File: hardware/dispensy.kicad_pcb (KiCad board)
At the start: 2 copper layers, 125 x 90 mm, 90 parts, among them SW1 BOOTSEL, SW2 RESET, U1 DBT50G-7_62-4P, U10 RP2040, U11 SS54, U12 SS54_C22452, U13 CAN_IO, U14 TJA1042T_3_1J, U15 USB-C, U16 LM2576S-5_0_TR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

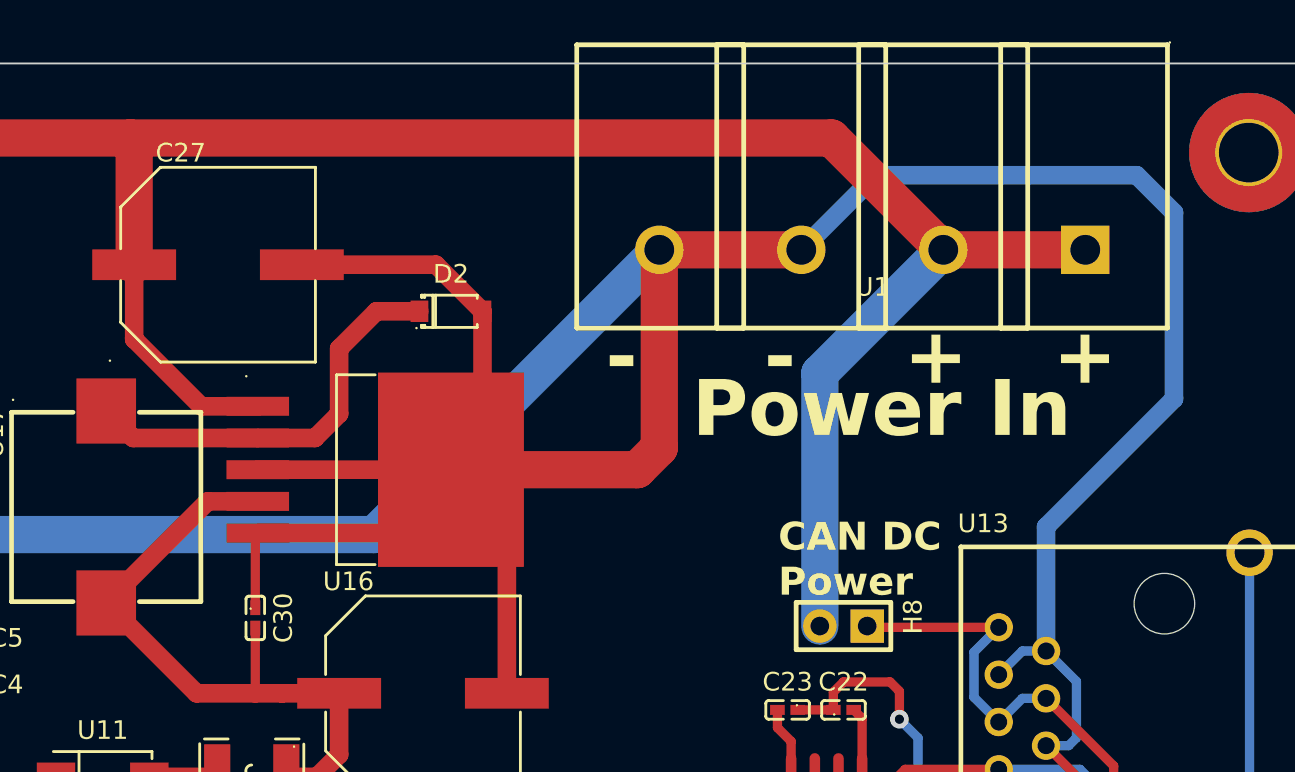
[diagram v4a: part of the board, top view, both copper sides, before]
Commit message: more distance between mounting hole and power connector.
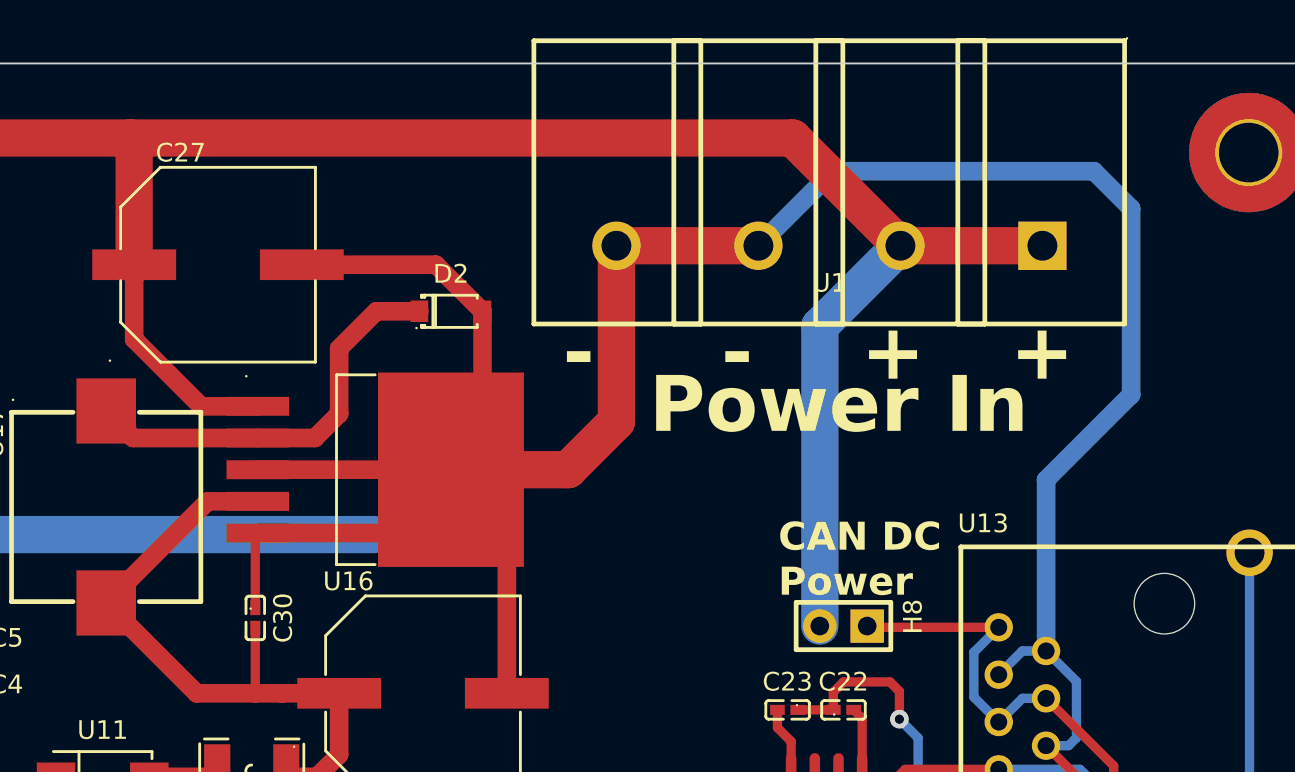
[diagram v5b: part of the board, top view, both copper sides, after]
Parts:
- moved U1 2.31 mm to (191.0, 57.5)
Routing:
- net GND: track 499.6 -> 474.3 mm
- net +VDC: track 126.2 -> 123.0 mm

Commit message: some more routing
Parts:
- moved C1 0.41 mm to (191.9, 109.8)
- moved OLED1 0.41 mm to (181.1, 137.0)
- moved R1 0.41 mm to (194.9, 109.8)
- moved R2 0.41 mm to (197.5, 109.8)
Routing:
- net +5V: track 37.0 -> 81.7 mm, vias 2 -> 8
- net GND: track 474.3 -> 498.2 mm

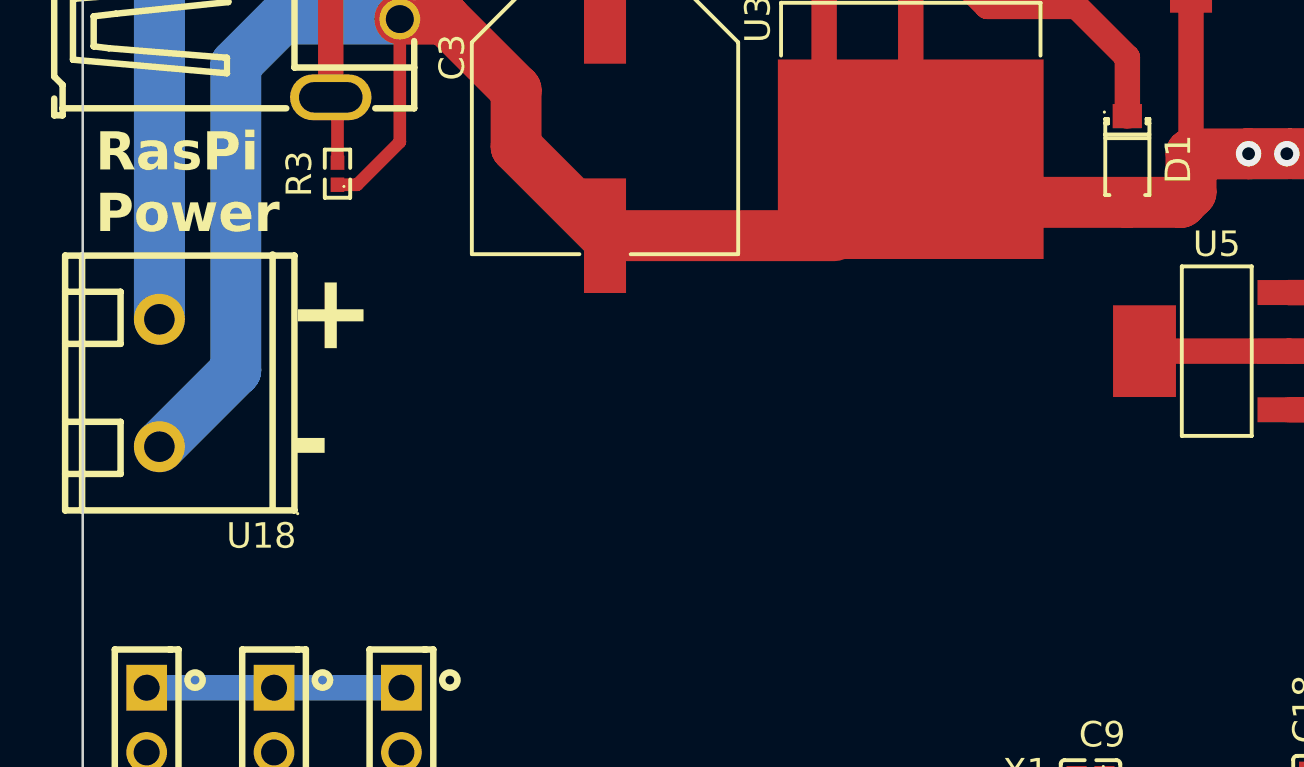
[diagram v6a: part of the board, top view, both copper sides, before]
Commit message: add power status leds
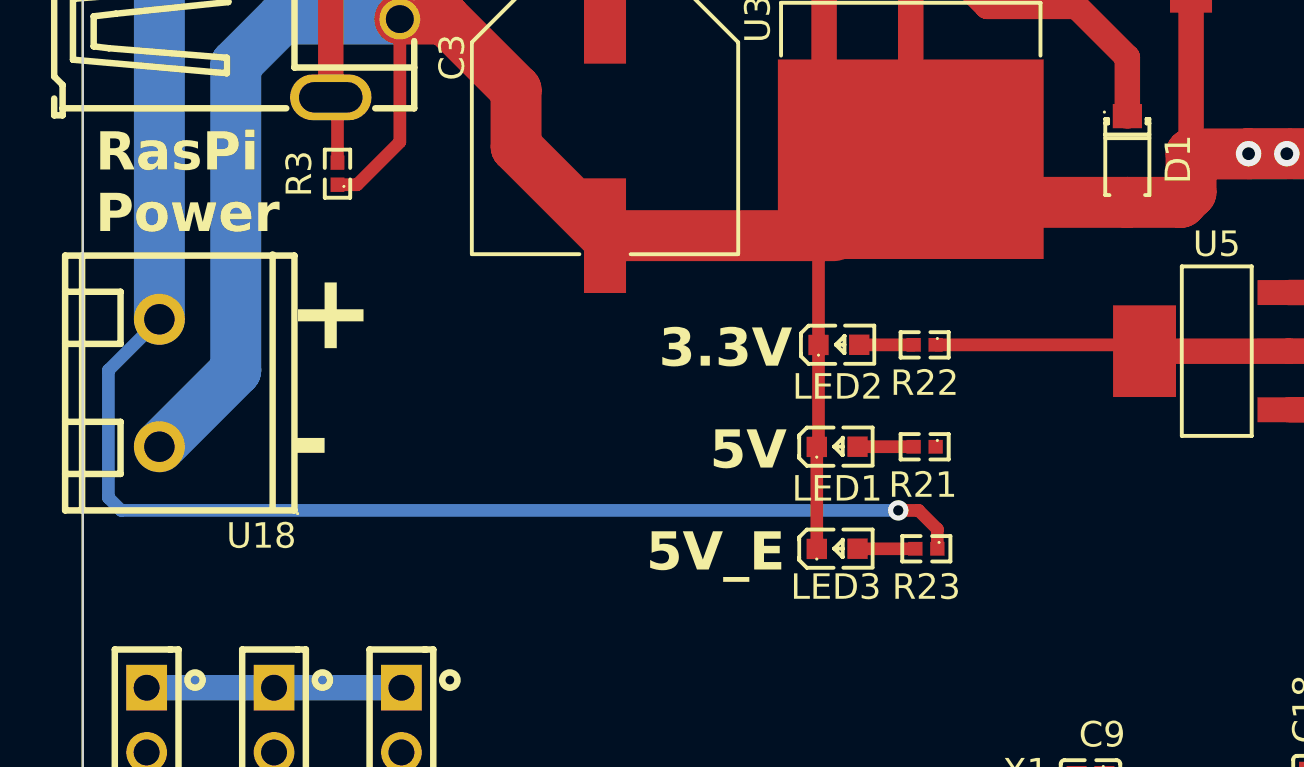
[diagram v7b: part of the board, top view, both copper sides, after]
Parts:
- added LED1: FC-D1608HGK-572C, jlc_footprints:LED0603-RD, F.Cu at (123.1, 84.5)
- added LED2: FC-D1608HGK-572C, jlc_footprints:LED0603-RD, F.Cu at (123.2, 80.5)
- added LED3: FC-D1608HGK-572C, jlc_footprints:LED0603-RD, F.Cu at (123.1, 88.5)
- added R21: 1K, jlc_footprints:R0402, F.Cu at (126.5, 84.5)
- added R22: 1K, jlc_footprints:R0402, F.Cu at (126.5, 80.5)
- added R23: 1K, jlc_footprints:R0402, F.Cu at (126.6, 88.5)
- U11: value SS54 -> SS54_C22452
- U5: value AMS1117-3_3 -> AMS1117-3_3_C347222
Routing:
- net Net-(U2-VCC): track 34.4 -> 76.0 mm, vias 0 -> 1
- net GND: track 498.2 -> 515.0 mm
- net +3.3V: track 128.5 -> 136.8 mm
- net Net-(LED3-+): track 0.00 -> 2.27 mm
- net Net-(LED1-+): track 0.00 -> 2.20 mm
- net Net-(LED2-+): track 0.00 -> 2.13 mm
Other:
- board text added: "3.3V"
- board text added: "5V"
- board text added: "5V_E"

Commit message: route more power connections
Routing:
- net +5V: track 81.7 -> 99.8 mm, vias 8 -> 10
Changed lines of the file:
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@@
   (title_block
     (title "Dispensy Mainboard")
-    (date "2024-01-21")
+    (date "2024-01-28")
     (rev "0")
     (company "DrinkRobotics")
@@
   (segment (start 146.5 120.5) (end 148 120.5) (width 1) (layer "F.Cu") (net 5))
   (segment (start 144.849886 120.650114) (end 145 120.5) (width 1) (layer "F.Cu") (net 5))
+  (segment (start 140.8349 78.450025) (end 138.950025 78.450025) (width 0.5) (layer "F.Cu") (net 5))
   (segment (start 168 120.5) (end 168 119.996317) (width 1) (layer "F.Cu") (net 5))
+  (segment (start 133 77.5) (end 132 78.5) (width 0.5) (layer "F.Cu") (net 5))
+  (segment (start 138.950025 78.450025) (end 138 77.5) (width 0.5) (layer "F.Cu") (net 5))
+  (segment (start 126.967615 84.503429) (end 127.496571 84.503429) (width 0.5) (layer "F.Cu") (net 5))
+  (segment (start 127.496571 84.503429) (end 128.5 83.5) (width 0.5) (layer "F.Cu") (net 5))
   (segment (start 140.8349 78.450025) (end 143.534925 78.450025) (width 1) (layer "F.Cu") (net 5))
   (segment (start 191.209881 81.45285) (end 191.754966 80.907765) (width 0.5) (layer "F.Cu") (net 5))
@@
   (segment (start 144.849886 122.850013) (end 144.849886 120.650114) (width 1) (layer "F.Cu") (net 5))
   (segment (start 194.254966 80.907765) (end 194.754966 81.407765) (width 0.5) (layer "F.Cu") (net 5))
+  (segment (start 138 77.5) (end 133 77.5) (width 0.5) (layer "F.Cu") (net 5))
   (segment (start 171 120.5) (end 171 119.996317) (width 1) (layer "F.Cu") (net 5))
   (segment (start 169.5 120.5) (end 171 120.5) (width 1) (layer "F.Cu") (net 5))
   (segment (start 146.5 120.5) (end 146.5 121.199899) (width 1) (layer "F.Cu") (net 5))
   (via (at 146.5 120.5) (size 1) (drill 0.5) (layers "F.Cu" "B.Cu") (net 5))
+  (via (at 132 78.5) (size 0.5) (drill 0.2) (layers "F.Cu" "B.Cu") (net 5))
   (via (at 195.754966 88.407765) (size 1) (drill 0.5) (layers "F.Cu" "B.Cu") (net 5))
   (via (at 194.754966 82.907765) (size 1) (drill 0.5) (layers "F.Cu" "B.Cu") (net 5))
   (via (at 171 120.5) (size 1) (drill 0.5) (layers "F.Cu" "B.Cu") (net 5))
+  (via (at 128.5 83.5) (size 0.5) (drill 0.2) (layers "F.Cu" "B.Cu") (net 5))
   (via (at 148 120.5) (size 1) (drill 0.5) (layers "F.Cu" "B.Cu") (net 5))
   (via (at 145 120.5) (size 1) (drill 0.5) (layers "F.Cu" "B.Cu") (net 5))
   (via (at 169.5 120.5) (size 1) (drill 0.5) (layers "F.Cu" "B.Cu") (net 5))
   (via (at 168 120.5) (size 1) (drill 0.5) (layers "F.Cu" "B.Cu") (net 5))
+  (segment (start 128.5 82) (end 128.5 83.5) (width 0.5) (layer "B.Cu") (net 5))
+  (segment (start 132 78.5) (end 128.5 82) (width 0.5) (layer "B.Cu") (net 5))
   (segment (start 195.754966 88.407765) (end 195.754966 83.907765) (width 0.5) (layer "B.Cu") (net 5))
   (segment (start 195.754966 83.907765) (end 194.754966 82.907765) (width 0.5) (layer "B.Cu") (net 5))
